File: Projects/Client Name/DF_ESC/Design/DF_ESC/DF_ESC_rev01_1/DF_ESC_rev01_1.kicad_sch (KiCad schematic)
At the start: 0 parts

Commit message: libraries & schemtics
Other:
- removed sheet OVERVIEW
- added sheet INPUT PROTECTION (INPUT PROTECTION.kicad_sch)
- added sheet STEP-DOWN (STEP-DOWN.kicad_sch)
- added sheet USB (USB.kicad_sch)
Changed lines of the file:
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@@
 		(title "DF_ESC_rev01_1")
 		(date "2025-01-29")
-		(rev "rev01")
+		(rev "rev01_1")
 		(company "coVenture")
 	)
@@
 	)
 	(sheet
-		(at 78.74 35.56)
+		(at 26.67 35.56)
 		(size 36.83 26.67)
 		(fields_autoplaced yes)
@@
 		)
 		(property "Sheetname" "BLOCK DIAGRAM"
-			(at 78.74 34.8484 0)
+			(at 26.67 34.8484 0)
 			(effects
 				(font
@@
 		)
 		(property "Sheetfile" "BLOCK DIAGRAM.kicad_sch"
-			(at 78.74 62.8146 0)
+			(at 26.67 62.8146 0)
 			(effects
 				(font
@@
 	)
 	(sheet
-		(at 27.94 35.56)
-		(size 35.56 26.67)
-		(fields_autoplaced yes)
-		(stroke
-			(width 0.1524)
-			(type solid)
-		)
-		(fill
-			(color 0 0 0 0.0000)
-		)
-		(property "Sheetname" "OVERVIEW"
-			(at 27.94 34.8484 0)
-			(effects
-				(font
-					(size 1.27 1.27)
-				)
-				(justify left bottom)
-			)
-		)
-		(property "Sheetfile" "OVERVIEW.kicad_sch"
-			(at 27.94 62.8146 0)
-			(effects
-				(font
-					(size 1.27 1.27)
-				)
-				(justify left top)
-			)
-		)
-		(instances
-			(project "DF_ESC_rev01_1"
-				(path "/e63e39d7-6ac0-4ffd-8aa3-1841a4541b55"
-					(page "6")
+		(at 27.94 128.27)
+		(size 34.29 33.02)
+		(fields_autoplaced yes)
+		(stroke
+			(width 0.1524)
+			(type solid)
+		)
+		(fill
+			(color 0 0 0 0.0000)
+		)
+		(property "Sheetname" "USB"
+			(at 27.94 127.5584 0)
+			(effects
+				(font
+					(size 1.27 1.27)
+				)
+				(justify left bottom)
+			)
+		)
+		(property "Sheetfile" "USB.kicad_sch"
+			(at 27.94 161.8746 0)
+			(effects
+				(font
+					(size 1.27 1.27)
+				)
+				(justify left top)
+			)
+		)
+		(instances
+			(project "DF_ESC_rev01_1"
+				(path "/e63e39d7-6ac0-4ffd-8aa3-1841a4541b55"
+					(page "11")
+				)
+			)
+		)
+	)
+	(sheet
+		(at 76.2 35.56)
+		(size 34.29 26.67)
+		(fields_autoplaced yes)
+		(stroke
+			(width 0.1524)
+			(type solid)
+		)
+		(fill
+			(color 0 0 0 0.0000)
+		)
+		(property "Sheetname" "INPUT PROTECTION"
+			(at 76.2 34.8484 0)
+			(effects
+				(font
+					(size 1.27 1.27)
+				)
+				(justify left bottom)
+			)
+		)
+		(property "Sheetfile" "INPUT PROTECTION.kicad_sch"
+			(at 76.2 62.8146 0)
+			(effects
+				(font
+					(size 1.27 1.27)
+				)
+				(justify left top)
+			)
+		)
+		(instances
+			(project "DF_ESC_rev01_1"
+				(path "/e63e39d7-6ac0-4ffd-8aa3-1841a4541b55"
+					(page "9")
 				)
 			)
@@
 	)
 	(sheet
+		(at 74.93 129.54)
+		(size 38.1 31.75)
+		(fields_autoplaced yes)
+		(stroke
+			(width 0.1524)
+			(type solid)
+		)
+		(fill
+			(color 0 0 0 0.0000)
+		)
+		(property "Sheetname" "MECHANICAL"
+			(at 74.93 128.8284 0)
+			(effects
+				(font
+					(size 1.27 1.27)
+				)
+				(justify left bottom)
+			)
+		)
+		(property "Sheetfile" "MECHANICAL.kicad_sch"
+			(at 74.93 161.8746 0)
+			(effects
+				(font
+					(size 1.27 1.27)
+				)
+				(justify left top)
+			)
+		)
+		(instances
+			(project "DF_ESC_rev01_1"
+				(path "/e63e39d7-6ac0-4ffd-8aa3-1841a4541b55"
+					(page "11")
+				)
+			)
+		)
+	)
+	(sheet
 		(at 125.73 85.09)
 		(size 35.56 26.67)
@@
 	)
 	(sheet
-		(at 27.94 127)
-		(size 36.83 33.02)
-		(fields_autoplaced yes)
-		(stroke
-			(width 0.1524)
-			(type solid)
-		)
-		(fill
-			(color 0 0 0 0.0000)
-		)
-		(property "Sheetname" "MECHANICAL"
-			(at 27.94 126.2884 0)
-			(effects
-				(font
-					(size 1.27 1.27)
-				)
-				(justify left bottom)
-			)
-		)
-		(property "Sheetfile" "MECHANICAL.kicad_sch"
-			(at 27.94 160.6046 0)
-			(effects
-				(font
-					(size 1.27 1.27)
-				)
-				(justify left top)
-			)
-		)
-		(instances
-			(project "DF_ESC_rev01_1"
-				(path "/e63e39d7-6ac0-4ffd-8aa3-1841a4541b55"
-					(page "9")
-				)
-			)
+		(at 124.46 35.56)
+		(size 36.83 27.94)
+		(fields_autoplaced yes)
+		(stroke
+			(width 0.1524)
+			(type solid)
+		)
+		(fill
+			(color 0 0 0 0.0000)
+		)
+		(property "Sheetname" "STEP-DOWN"
+			(at 124.46 34.8484 0)
+			(effects
+				(font
+					(size 1.27 1.27)
+				)
+				(justify left bottom)
+			)
+		)
+		(property "Sheetfile" "STEP-DOWN.kicad_sch"
+			(at 124.46 64.0846 0)
+			(effects
+				(font
+					(size 1.27 1.27)
+				)
+				(justify left top)
+			)
+		)
+		(instances
+			(project "DF_ESC_rev01_1"
+				(path "/e63e39d7-6ac0-4ffd-8aa3-1841a4541b55"
+					(page "10")
+				)
+			)

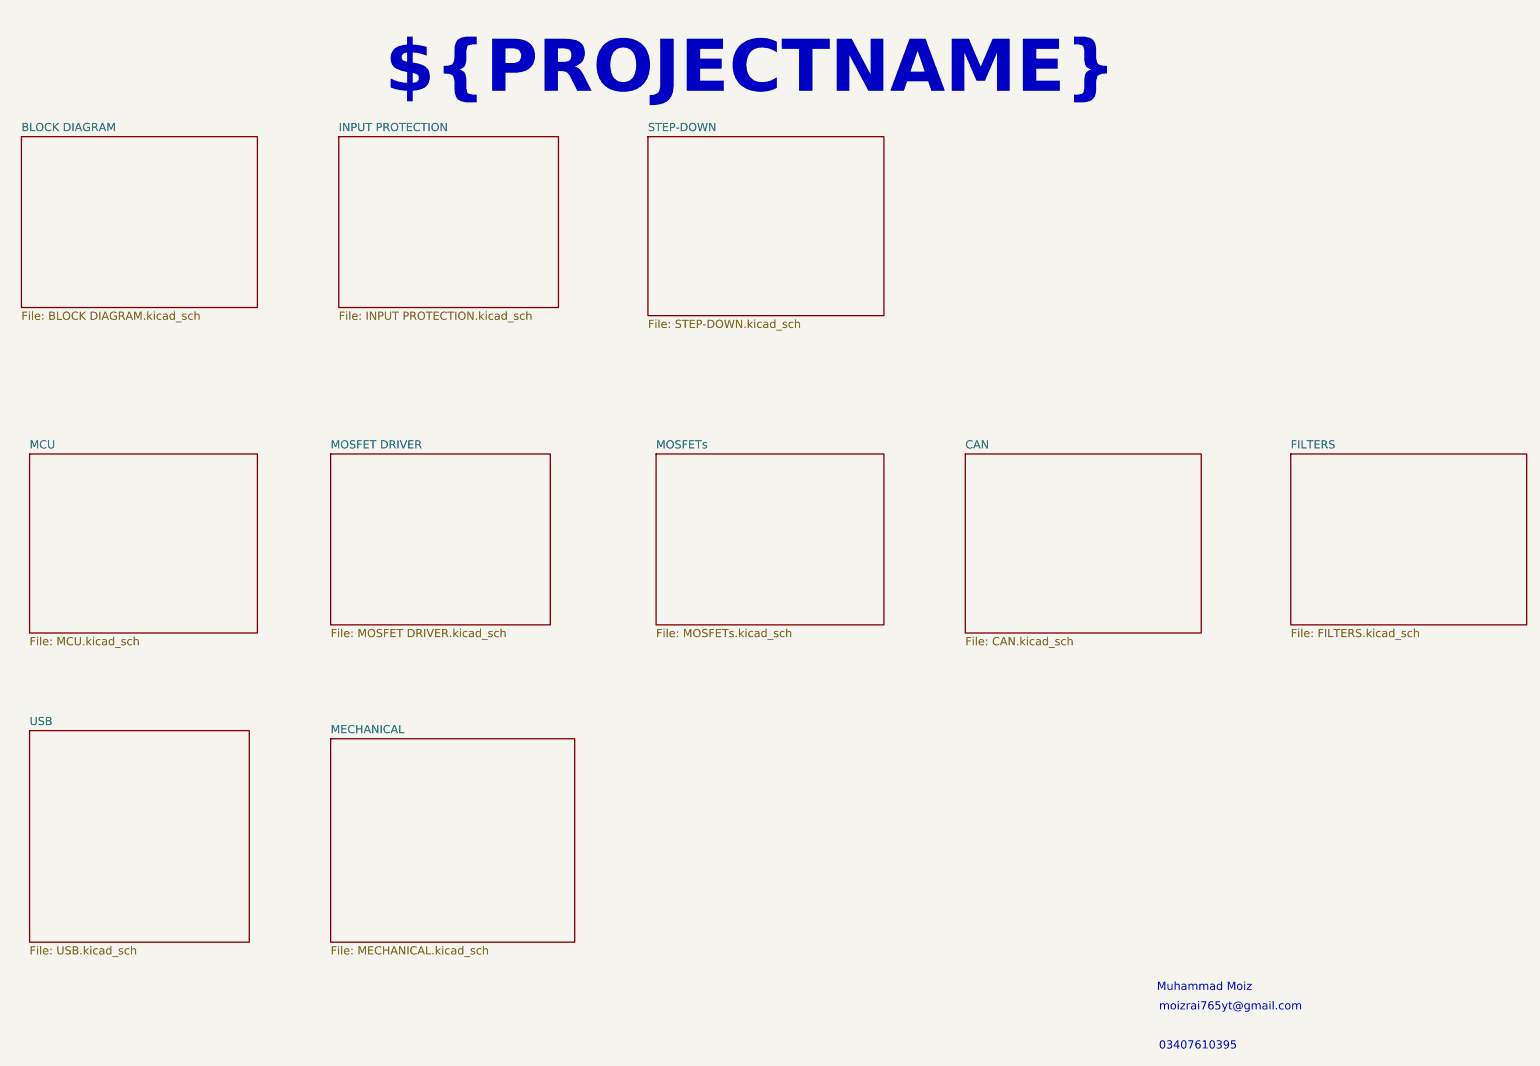
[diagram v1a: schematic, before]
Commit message: updated footprints
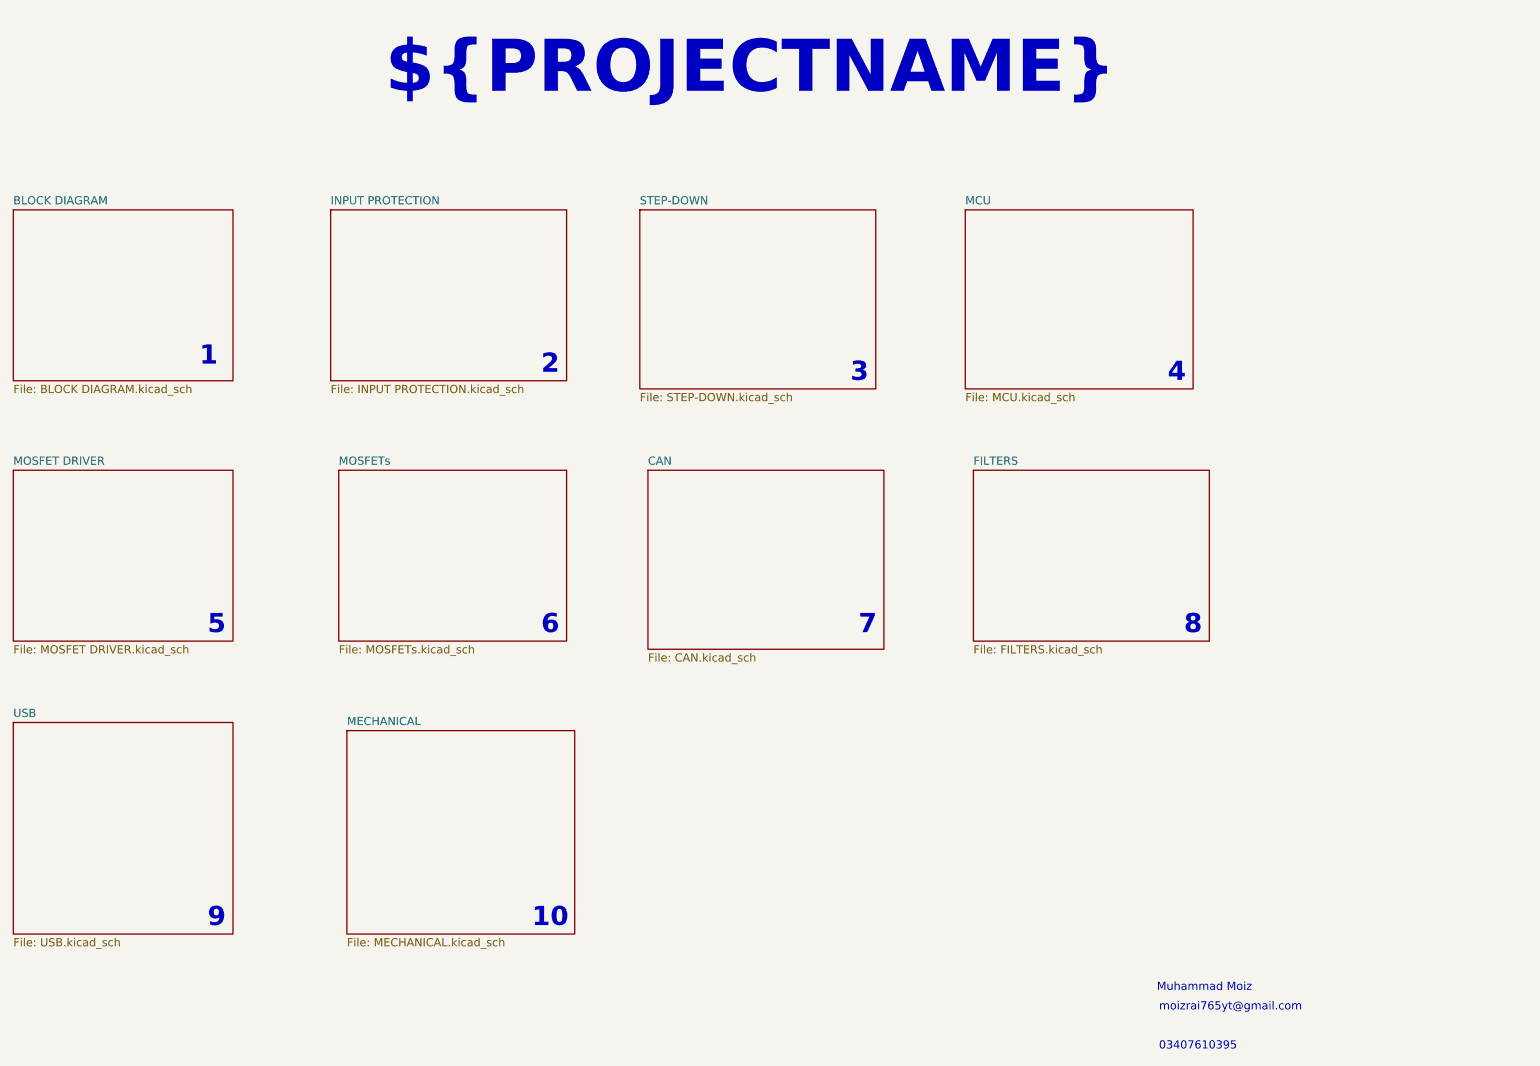
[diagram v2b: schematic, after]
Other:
- note added: "1"
- note added: "10"
- note added: "2"
- note added: "3"
- note added: "4"
- note added: "5"
- note added: "6"
- note added: "7"
- note added: "8"
- note added: "9"
